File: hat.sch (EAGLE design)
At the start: 9 parts, among them U1 CAT24C32

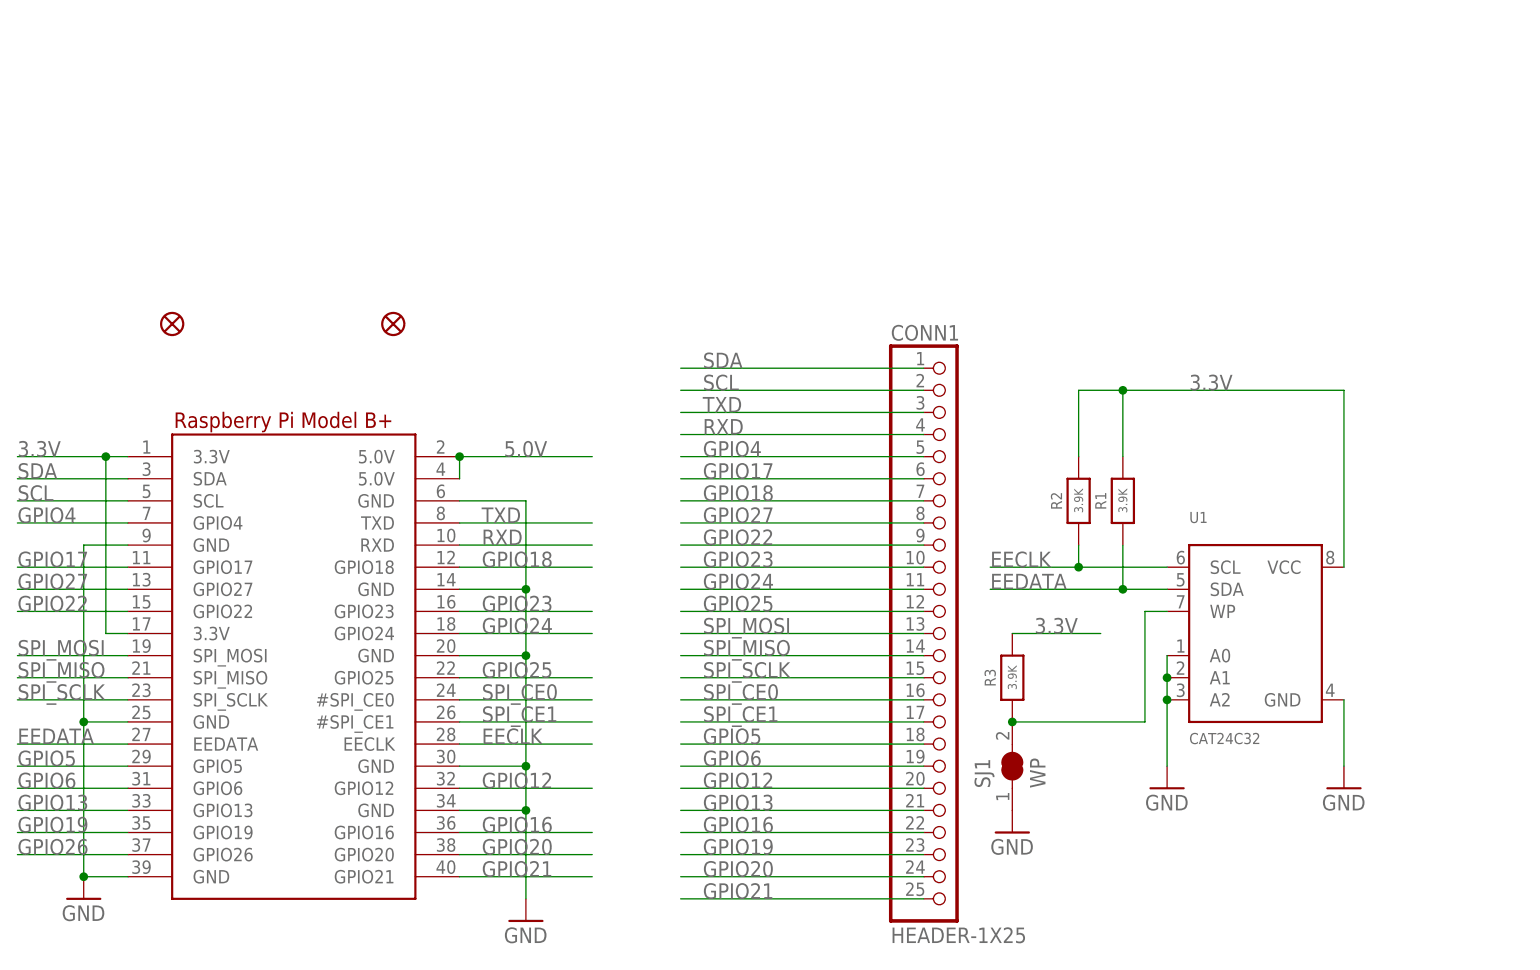
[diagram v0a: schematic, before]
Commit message: simple connector breakout board
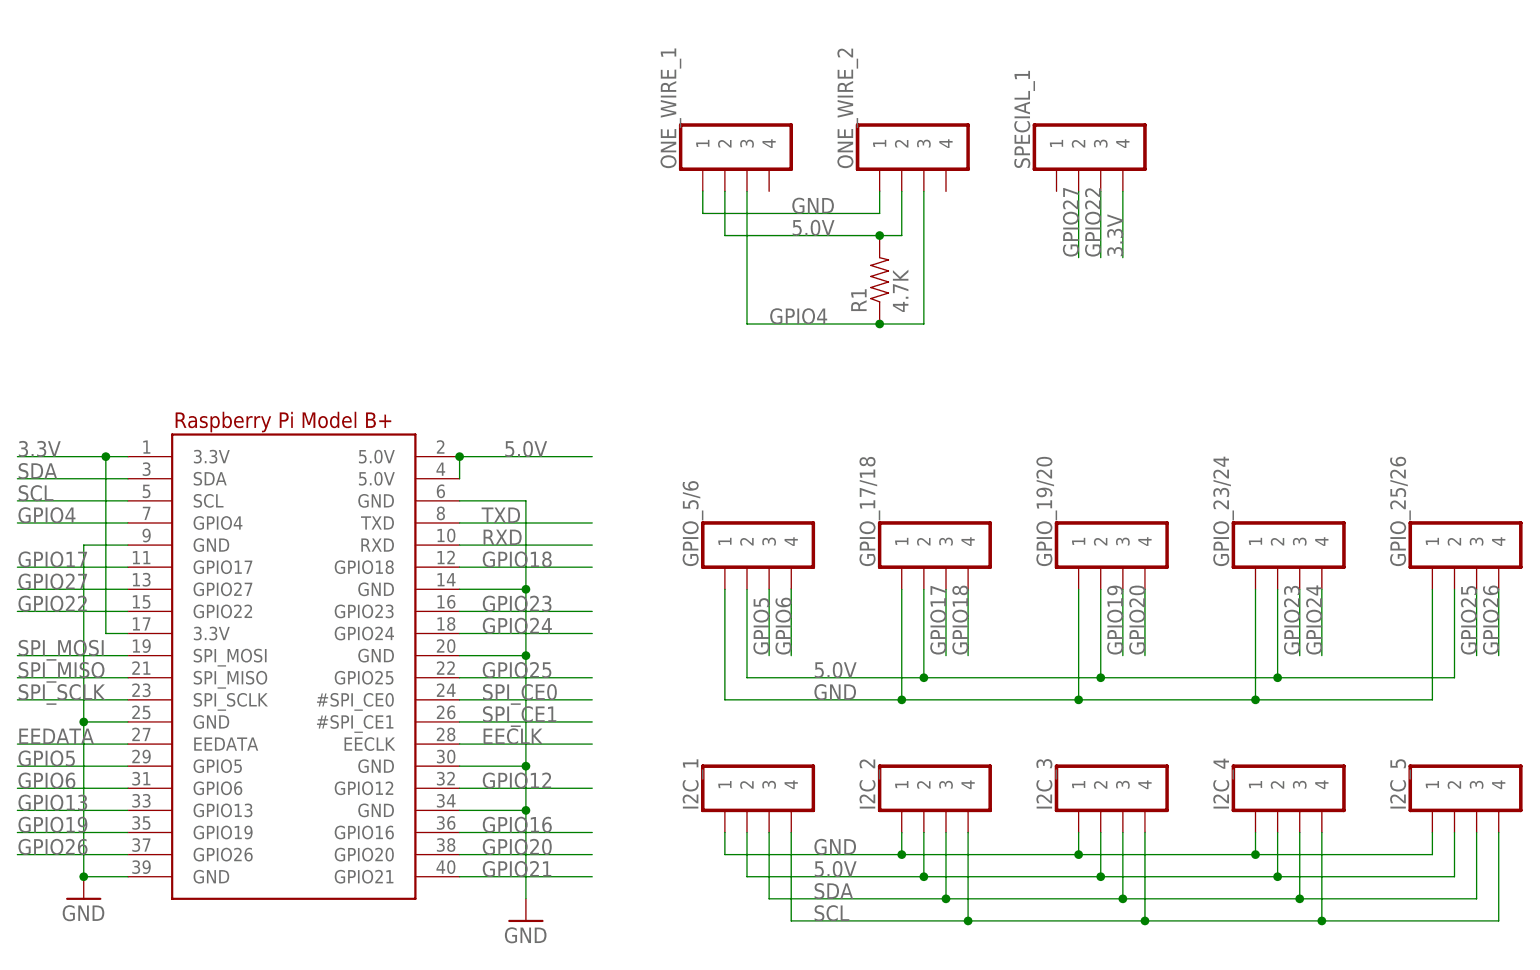
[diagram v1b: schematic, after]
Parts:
- removed CONN1: HEADER-1X25, microbuilder:HEADER-1X25
- removed FID2, FID3: FIDUCIAL"", microbuilder:FIDUCIAL""
- removed R2, R3: 3.9K, microbuilder:RESISTOR0805_NOOUTLINE
- removed SJ1: WP, microbuilder:SOLDERJUMPER_CLOSED
- removed U1: CAT24C32, microbuilder:EEPROM_I2C_SOIC8_GENERIC
- added GPIO_17/18, GPIO_19/20, GPIO_23/24, GPIO_25/26, GPIO_5/6, I2C_1, I2C_2, I2C_3, I2C_4, I2C_5, ONE_WIRE_1, ONE_WIRE_2, SPECIAL_1: MOLEX_0705430003, REM_Connectors_Molex:MOLEX_0705430003
- R1: value 3.9K -> 4.7K; device microbuilder:RESISTOR0805_NOOUTLINE -> SparkFun:RESISTORPTH1
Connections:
- removed net N$16: R3.1, SJ1.2, U1.WP
- net 3.3V: now also SPECIAL_1.4; no longer R1.2, R2.2, R3.2, U1.VCC
- net 5.0V: now also GPIO_17/18.2, GPIO_19/20.2, GPIO_23/24.2, GPIO_25/26.2, GPIO_5/6.2, I2C_1.2, I2C_2.2, I2C_3.2, I2C_4.2, I2C_5.2, ONE_WIRE_1.2, ONE_WIRE_2.2, R1.2
- net EECLK: no longer R2.1, U1.SCL
- net EEDATA: no longer R1.1, U1.SDA
- net GND: now also GPIO_17/18.1, GPIO_19/20.1, GPIO_23/24.1, GPIO_25/26.1, GPIO_5/6.1, I2C_1.1, I2C_2.1, I2C_3.1, I2C_4.1, I2C_5.1, ONE_WIRE_1.1, ONE_WIRE_2.1; no longer SJ1.1, U1.A0, U1.A1, U1.A2, U1.GND
- net GPIO12: no longer CONN1.20
- net GPIO13: no longer CONN1.21
- net GPIO16: no longer CONN1.22
- net GPIO17: now also GPIO_17/18.3; no longer CONN1.6
- net GPIO18: now also GPIO_17/18.4; no longer CONN1.7
- net GPIO19: now also GPIO_19/20.3; no longer CONN1.23
- net GPIO20: now also GPIO_19/20.4; no longer CONN1.24
- net GPIO21: no longer CONN1.25
- net GPIO22: now also SPECIAL_1.3; no longer CONN1.9
- net GPIO23: now also GPIO_23/24.3; no longer CONN1.10
- net GPIO24: now also GPIO_23/24.4; no longer CONN1.11
- net GPIO25: now also GPIO_25/26.3; no longer CONN1.12
- net GPIO26: now also GPIO_25/26.4
- net GPIO27: now also SPECIAL_1.2; no longer CONN1.8
- net GPIO4: now also ONE_WIRE_1.3, ONE_WIRE_2.3, R1.1; no longer CONN1.5
- net GPIO5: now also GPIO_5/6.3; no longer CONN1.18
- net GPIO6: now also GPIO_5/6.4; no longer CONN1.19
- net RXD: no longer CONN1.4
- net SCL: now also I2C_1.4, I2C_2.4, I2C_3.4, I2C_4.4, I2C_5.4; no longer CONN1.2
- net SDA: now also I2C_1.3, I2C_2.3, I2C_3.3, I2C_4.3, I2C_5.3; no longer CONN1.1
- net SPI_CE0: no longer CONN1.16
- net SPI_CE1: no longer CONN1.17
- net SPI_MISO: no longer CONN1.14
- net SPI_MOSI: no longer CONN1.13
- net SPI_SCLK: no longer CONN1.15
- net TXD: no longer CONN1.3
